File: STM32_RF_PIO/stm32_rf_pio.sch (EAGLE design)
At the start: 10 parts, among them IC1 ULN2804A, IC2 ULN2804A, IC3 ULN2804A, X1 22-23-2081, X2 22-23-2081, X3 22-23-2081, X4 Outputs Power

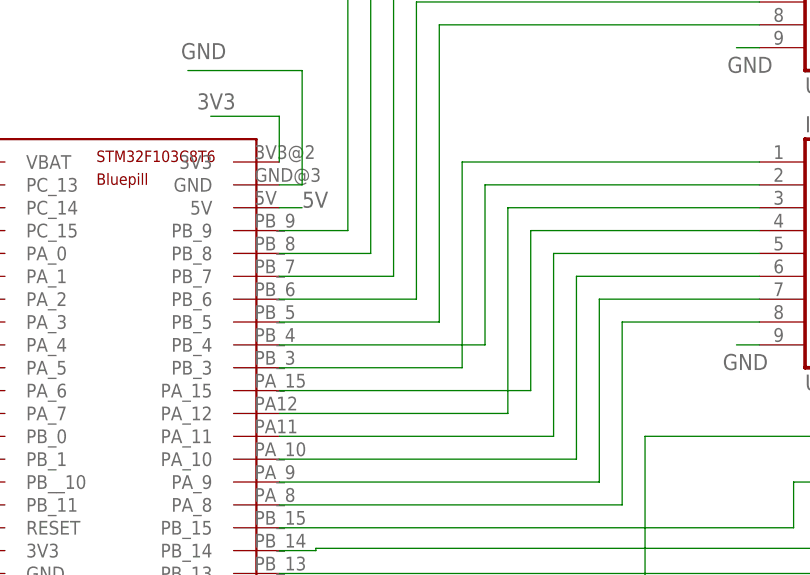
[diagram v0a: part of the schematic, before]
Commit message: Added connections for servo motors with Gnd-HV-Signal for all pwm outputs
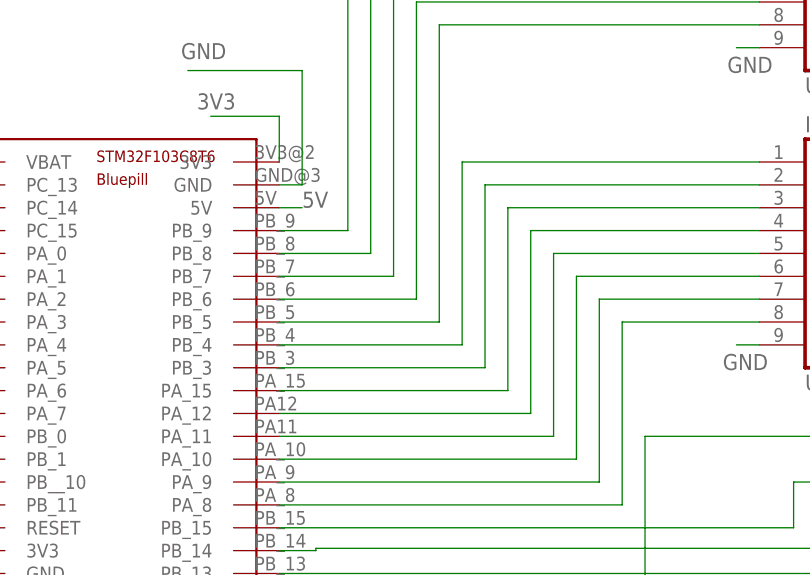
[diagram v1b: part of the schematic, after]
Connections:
- net N$53 renamed HV
- net A12: now also IC1.I4; no longer IC1.I3
- net M21: now also IC1.I3; no longer IC1.I4
- net M22: now also IC1.I2; no longer IC1.I1
- net M31: now also IC1.I1; no longer IC1.I2
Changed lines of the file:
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@@
+</segment>
+</net>
+<net name="A12" class="0">
+<segment>
+<pinref part="IC1" gate="G$1" pin="I4"/>
+<wire x1="7.62" y1="-5.08" x2="7.62" y2="15.24" width="0.1524" layer="91"/>
+<wire x1="7.62" y1="15.24" x2="33.02" y2="15.24" width="0.1524" layer="91"/>
+<pinref part="U$1" gate="G$1" pin="PA_12"/>
+<wire x1="7.62" y1="-5.08" x2="-20.32" y2="-5.08" width="0.1524" layer="91"/>
 </segment>
 </net>
 <net name="M21" class="0">
 <segment>
-<pinref part="IC1" gate="G$1" pin="I4"/>
-<wire x1="7.62" y1="-2.54" x2="7.62" y2="15.24" width="0.1524" layer="91"/>
-<wire x1="7.62" y1="15.24" x2="33.02" y2="15.24" width="0.1524" layer="91"/>
+<pinref part="IC1" gate="G$1" pin="I3"/>
+<wire x1="5.08" y1="-2.54" x2="5.08" y2="17.78" width="0.1524" layer="91"/>
+<wire x1="5.08" y1="17.78" x2="33.02" y2="17.78" width="0.1524" layer="91"/>
 <pinref part="U$1" gate="G$1" pin="PA_15"/>
-<wire x1="-20.32" y1="-2.54" x2="7.62" y2="-2.54" width="0.1524" layer="91"/>
-</segment>
-</net>
-<net name="A12" class="0">
-<segment>
-<wire x1="5.08" y1="-5.08" x2="5.08" y2="17.78" width="0.1524" layer="91"/>
-<pinref part="IC1" gate="G$1" pin="I3"/>
-<wire x1="5.08" y1="17.78" x2="33.02" y2="17.78" width="0.1524" layer="91"/>
-<pinref part="U$1" gate="G$1" pin="PA_12"/>
-<wire x1="5.08" y1="-5.08" x2="-20.32" y2="-5.08" width="0.1524" layer="91"/>
-</segment>
-</net>
-<net name="M31" class="0">
+<wire x1="5.08" y1="-2.54" x2="-20.32" y2="-2.54" width="0.1524" layer="91"/>
+</segment>
+</net>
+<net name="M22" class="0">
 <segment>
 <pinref part="IC1" gate="G$1" pin="I2"/>
 <wire x1="33.02" y1="20.32" x2="2.54" y2="20.32" width="0.1524" layer="91"/>
-<wire x1="2.54" y1="20.32" x2="2.54" y2="2.54" width="0.1524" layer="91"/>
+<wire x1="2.54" y1="20.32" x2="2.54" y2="0" width="0.1524" layer="91"/>
+<pinref part="U$1" gate="G$1" pin="PB_3"/>
+<wire x1="2.54" y1="0" x2="-20.32" y2="0" width="0.1524" layer="91"/>
+</segment>
+</net>
+<net name="M31" class="0">
+<segment>
+<pinref part="IC1" gate="G$1" pin="I1"/>
+<wire x1="0" y1="2.54" x2="0" y2="22.86" width="0.1524" layer="91"/>
+<wire x1="0" y1="22.86" x2="33.02" y2="22.86" width="0.1524" layer="91"/>
 <pinref part="U$1" gate="G$1" pin="PB_4"/>
-<wire x1="2.54" y1="2.54" x2="-20.32" y2="2.54" width="0.1524" layer="91"/>
-</segment>
-</net>
-<net name="M22" class="0">
-<segment>
-<wire x1="0" y1="0" x2="0" y2="22.86" width="0.1524" layer="91"/>
-<pinref part="IC1" gate="G$1" pin="I1"/>
-<wire x1="0" y1="22.86" x2="33.02" y2="22.86" width="0.1524" layer="91"/>
-<pinref part="U$1" gate="G$1" pin="PB_3"/>
-<wire x1="0" y1="0" x2="-20.32" y2="0" width="0.1524" layer="91"/>
+<wire x1="-20.32" y1="2.54" x2="0" y2="2.54" width="0.1524" layer="91"/>
 </segment>
 </net>
@@
 </segment>
 </net>
-<net name="N$53" class="0">
+<net name="HV" class="0">
 <segment>
 <pinref part="X4" gate="-2" pin="KL"/>
